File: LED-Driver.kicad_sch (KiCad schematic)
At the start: 9 parts, among them J1 Conn_01x04, J2 Barrel_Jack, Q1 Q_NPN_ECB, Q2 Q_NPN_ECB, Q3 Q_NPN_ECB, U1 Pico

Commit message: Add an initial PCB and swap out the barrel jack
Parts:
- removed J2: Barrel_Jack, Connector_BarrelJack:BarrelJack_SwitchcraftConxall_RAPC10U_Horizontal, symbol Connector:Barrel_Jack
- added J2: Barrel_Jack_Switch, Connector_BarrelJack:BarrelJack_CUI_PJ-102AH_Horizontal, symbol Connector:Barrel_Jack_Switch
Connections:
- net +12V: now also J2.1
- net GND: now also J2.2
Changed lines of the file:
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@@
+	)
+	(symbol
+		(lib_id "Connector:Barrel_Jack_Switch")
+		(at 25.4 88.9 0)
+		(unit 1)
+		(exclude_from_sim no)
+		(in_bom yes)
+		(on_board yes)
+		(dnp no)
+		(fields_autoplaced yes)
+		(property "Reference" "J2"
+			(at 25.4 80.01 0)
+			(effects
+				(font
+					(size 1.27 1.27)
+				)
+			)
+		)
+		(property "Value" "Barrel_Jack_Switch"
+			(at 25.4 82.55 0)
+			(effects
+				(font
+					(size 1.27 1.27)
+				)
+			)
+		)
+		(property "Footprint" "Connector_BarrelJack:BarrelJack_CUI_PJ-102AH_Horizontal"
+			(at 26.67 89.916 0)
+			(effects
+				(font
+					(size 1.27 1.27)
+				)
+				(hide yes)
+			)
+		)
+		(property "Datasheet" "~"
+			(at 26.67 89.916 0)
+			(effects
+				(font
+					(size 1.27 1.27)
+				)
+				(hide yes)
+			)
+		)
+		(property "Description" "DC Barrel Jack with an internal switch"
+			(at 25.4 88.9 0)
+			(effects
+				(font
+					(size 1.27 1.27)
+				)
+				(hide yes)
+			)
+		)
+		(pin "3"
+		)
+		(pin "2"
+		)
+		(pin "1"
+		)
+		(instances
+			(project ""
+				(path "/1411000f-ec3e-4037-9ea8-3f20f090e81e"
+					(reference "J2")
+					(unit 1)
+				)
+			)
+		)
 	)
 	(symbol
@@
 					(unit 1)
 				)
-			)
-		)
-	)
-	(symbol
-		(lib_id "Connector:Barrel_Jack")
-		(at 25.4 88.9 0)
-		(unit 1)
-		(exclude_from_sim no)
-		(in_bom yes)
-		(on_board yes)
-		(dnp no)
-		(fields_autoplaced yes)
-		(property "Reference" "J2"
-			(at 25.4 80.01 0)
-			(effects
-				(font
-					(size 1.27 1.27)
-				)
-			)
-		)
-		(property "Value" "Barrel_Jack"
-			(at 25.4 82.55 0)
-			(effects
-				(font
-					(size 1.27 1.27)
-				)
-			)
-		)
-		(property "Footprint" "Connector_BarrelJack:BarrelJack_SwitchcraftConxall_RAPC10U_Horizontal"
-			(at 26.67 89.916 0)
-			(effects
-				(font
-					(size 1.27 1.27)
-				)
-				(hide yes)
-			)
-		)
-		(property "Datasheet" "~"
-			(at 26.67 89.916 0)
-			(effects
-				(font
-					(size 1.27 1.27)
-				)
-				(hide yes)
-			)
-		)
-		(property "Description" "DC Barrel Jack"
-			(at 25.4 88.9 0)
-			(effects
-				(font
-					(size 1.27 1.27)
-				)
-				(hide yes)
-			)
-		)
-		(pin "1"
-		)
-		(pin "2"
-		)
-		(instances
-			(project ""
-				(path "/1411000f-ec3e-4037-9ea8-3f20f090e81e"
-					(reference "J2")
-					(unit 1)
-				)

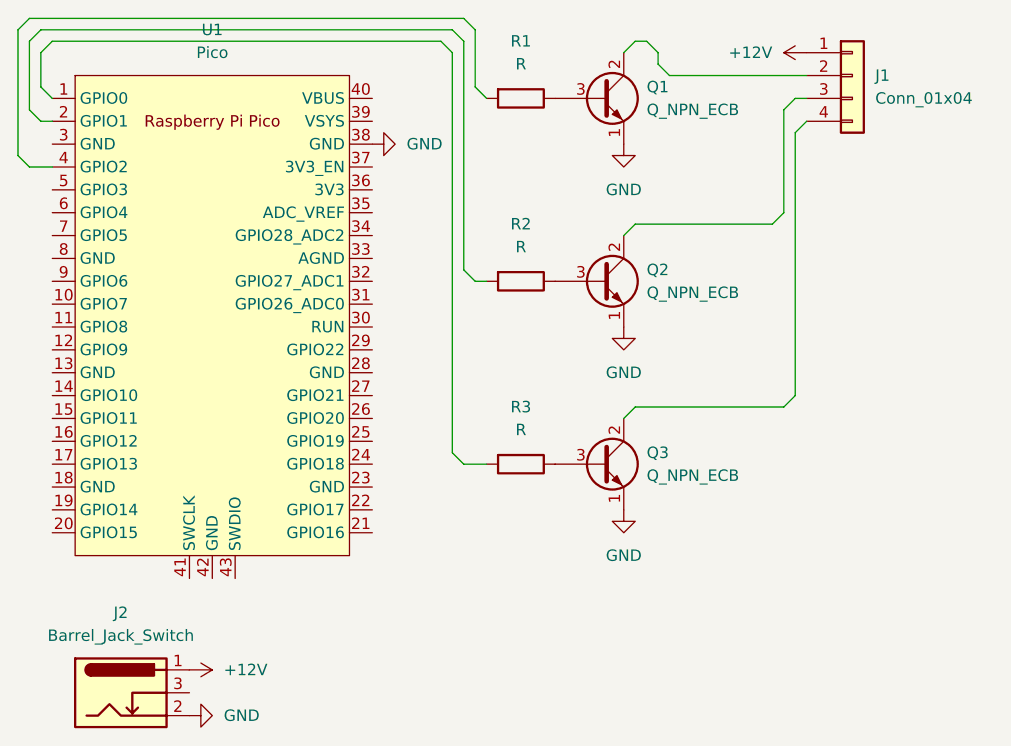
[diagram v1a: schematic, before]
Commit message: Add borders to the PCB
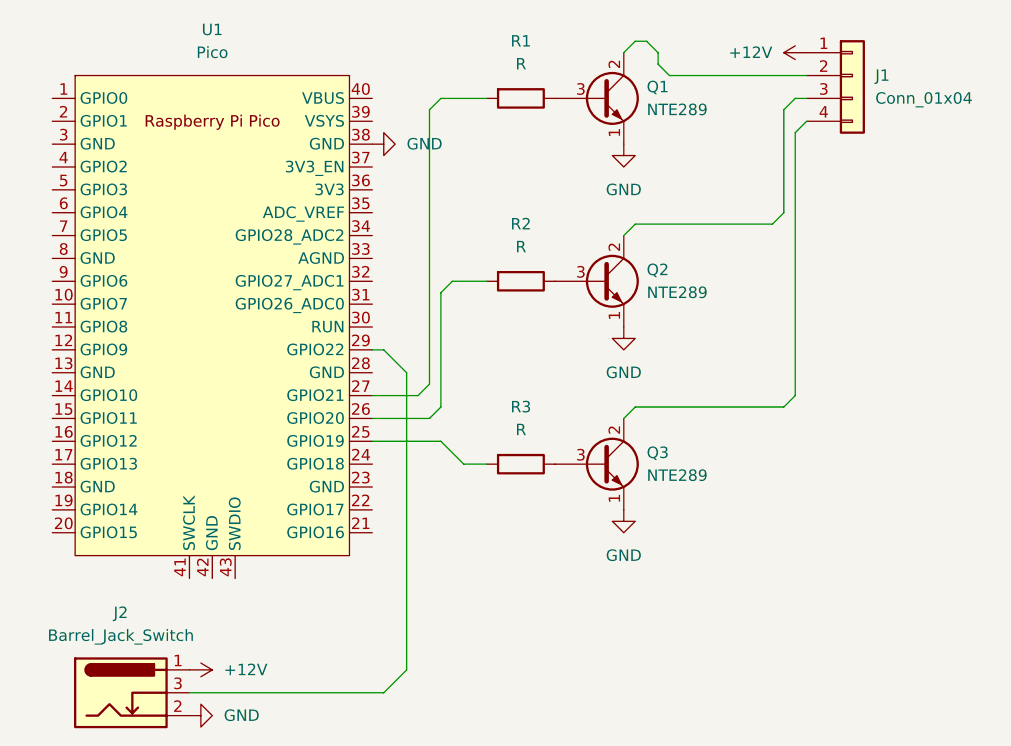
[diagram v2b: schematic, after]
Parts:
- J1: footprint (none) -> Connector_PinHeader_2.54mm:PinHeader_1x04_P2.54mm_Horizontal
- Q1, Q2, Q3: value Q_NPN_ECB -> NTE289; footprint (none) -> Package_TO_SOT_THT:TO-92_Inline
- R1, R2, R3: footprint (none) -> Resistor_THT:R_Axial_DIN0207_L6.3mm_D2.5mm_P10.16mm_Horizontal
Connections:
- net at R2.2: now also U1.26 (GPIO20); no longer U1.2 (GPIO1)
- net at U1.1 (GPIO0): no longer R3.2
- net at U1.25 (GPIO19): now also R3.2
- net at U1.27 (GPIO21): now also R1.2
- net at U1.29 (GPIO22): now also J2.3
- net at U1.4 (GPIO2): no longer R1.2
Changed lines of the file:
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@@
+	(wire
+		(pts
+			(xy 60.96 57.15) (xy 60.96 44.45)
+		)
+		(stroke
+			(width 0)
+			(type default)
+		)
+	)
 	(wire
 		(pts
@@
 	(wire
 		(pts
-			(xy 17.78 22.86) (xy 16.51 21.59)
-		)
-		(stroke
-			(width 0)
-			(type default)
-		)
-	)
-	(wire
-		(pts
-			(xy 64.77 43.18) (xy 63.5 41.91)
-		)
-		(stroke
-			(width 0)
-			(type default)
-		)
-	)
-	(wire
-		(pts
-			(xy 16.51 15.24) (xy 62.23 15.24)
+			(xy 58.42 55.88) (xy 59.69 54.61)
 		)
 		(stroke
@@
 	(wire
 		(pts
-			(xy 13.97 29.21) (xy 13.97 15.24)
-		)
-		(stroke
-			(width 0)
-			(type default)
-		)
-	)
-	(wire
-		(pts
 			(xy 82.55 16.51) (xy 83.82 16.51)
 		)
@@
 	(wire
 		(pts
-			(xy 64.77 15.24) (xy 63.5 13.97)
+			(xy 60.96 60.96) (xy 63.5 63.5)
 		)
 		(stroke
@@
 	(wire
 		(pts
-			(xy 13.97 15.24) (xy 15.24 13.97)
-		)
-		(stroke
-			(width 0)
-			(type default)
-		)
-	)
-	(wire
-		(pts
 			(xy 82.55 57.15) (xy 81.28 58.42)
 		)
@@
 	(wire
 		(pts
-			(xy 17.78 30.48) (xy 15.24 30.48)
+			(xy 53.34 50.8) (xy 54.61 50.8)
+		)
+		(stroke
+			(width 0)
+			(type default)
+		)
+	)
+	(wire
+		(pts
+			(xy 53.34 55.88) (xy 58.42 55.88)
 		)
 		(stroke
@@
 	(wire
 		(pts
-			(xy 15.24 13.97) (xy 63.5 13.97)
-		)
-		(stroke
-			(width 0)
-			(type default)
-		)
-	)
-	(wire
-		(pts
-			(xy 62.23 17.78) (xy 60.96 16.51)
-		)
-		(stroke
-			(width 0)
-			(type default)
-		)
-	)
-	(wire
-		(pts
-			(xy 15.24 16.51) (xy 16.51 15.24)
-		)
-		(stroke
-			(width 0)
-			(type default)
-		)
-	)
-	(wire
-		(pts
-			(xy 16.51 25.4) (xy 15.24 24.13)
-		)
-		(stroke
-			(width 0)
-			(type default)
-		)
-	)
-	(wire
-		(pts
-			(xy 66.04 43.18) (xy 64.77 43.18)
-		)
-		(stroke
-			(width 0)
-			(type default)
-		)
-	)
-	(wire
-		(pts
-			(xy 66.04 22.86) (xy 64.77 21.59)
-		)
-		(stroke
-			(width 0)
-			(type default)
-		)
-	)
-	(wire
-		(pts
-			(xy 16.51 17.78) (xy 17.78 16.51)
-		)
-		(stroke
-			(width 0)
-			(type default)
-		)
-	)
-	(wire
-		(pts
-			(xy 15.24 30.48) (xy 13.97 29.21)
-		)
-		(stroke
-			(width 0)
-			(type default)
-		)
-	)
-	(wire
-		(pts
-			(xy 17.78 25.4) (xy 16.51 25.4)
-		)
-		(stroke
-			(width 0)
-			(type default)
-		)
-	)
-	(wire
-		(pts
-			(xy 63.5 41.91) (xy 63.5 16.51)
-		)
-		(stroke
-			(width 0)
-			(type default)
-		)
-	)
-	(wire
-		(pts
-			(xy 63.5 16.51) (xy 62.23 15.24)
+			(xy 59.69 24.13) (xy 60.96 22.86)
 		)
 		(stroke
@@
 	(wire
 		(pts
+			(xy 60.96 22.86) (xy 66.04 22.86)
+		)
+		(stroke
+			(width 0)
+			(type default)
+		)
+	)
+	(wire
+		(pts
 			(xy 83.82 16.51) (xy 85.09 17.78)
 		)
@@
 	(wire
 		(pts
-			(xy 63.5 63.5) (xy 62.23 62.23)
-		)
-		(stroke
-			(width 0)
-			(type default)
-		)
-	)
-	(wire
-		(pts
 			(xy 81.28 17.78) (xy 82.55 16.51)
 		)
@@
 	(wire
 		(pts
-			(xy 64.77 21.59) (xy 64.77 15.24)
+			(xy 62.23 43.18) (xy 66.04 43.18)
 		)
 		(stroke
@@
 	(wire
 		(pts
-			(xy 16.51 17.78) (xy 16.51 21.59)
+			(xy 53.34 60.96) (xy 60.96 60.96)
 		)
 		(stroke
@@
 	(wire
 		(pts
+			(xy 57.15 53.34) (xy 57.15 86.36)
+		)
+		(stroke
+			(width 0)
+			(type default)
+		)
+	)
+	(wire
+		(pts
+			(xy 54.61 50.8) (xy 57.15 53.34)
+		)
+		(stroke
+			(width 0)
+			(type default)
+		)
+	)
+	(wire
+		(pts
 			(xy 99.06 57.15) (xy 82.55 57.15)
 		)
@@
 	(wire
 		(pts
+			(xy 59.69 54.61) (xy 59.69 24.13)
+		)
+		(stroke
+			(width 0)
+			(type default)
+		)
+	)
+	(wire
+		(pts
 			(xy 85.09 17.78) (xy 85.09 19.05)
 		)
@@
 	(wire
 		(pts
+			(xy 53.34 58.42) (xy 59.69 58.42)
+		)
+		(stroke
+			(width 0)
+			(type default)
+		)
+	)
+	(wire
+		(pts
 			(xy 100.33 26.67) (xy 100.33 55.88)
 		)
@@
 	(wire
 		(pts
-			(xy 15.24 24.13) (xy 15.24 16.51)
-		)
-		(stroke
-			(width 0)
-			(type default)
-		)
-	)
-	(wire
-		(pts
-			(xy 62.23 62.23) (xy 62.23 17.78)
-		)
-		(stroke
-			(width 0)
-			(type default)
-		)
-	)
-	(wire
-		(pts
-			(xy 17.78 16.51) (xy 60.96 16.51)
+			(xy 60.96 44.45) (xy 62.23 43.18)
+		)
+		(stroke
+			(width 0)
+			(type default)
+		)
+	)
+	(wire
+		(pts
+			(xy 57.15 86.36) (xy 54.61 88.9)
+		)
+		(stroke
+			(width 0)
+			(type default)
+		)
+	)
+	(wire
+		(pts
+			(xy 33.02 88.9) (xy 54.61 88.9)
+		)
+		(stroke
+			(width 0)
+			(type default)
+		)
+	)
+	(wire
+		(pts
+			(xy 59.69 58.42) (xy 60.96 57.15)
 		)
 		(stroke
@@
 			)
 		)
-		(property "Footprint" ""
+		(property "Footprint" "Resistor_THT:R_Axial_DIN0207_L6.3mm_D2.5mm_P10.16mm_Horizontal"
 			(at 69.85 41.402 90)
 			(effects
@@
 			)
 		)
-		(property "Footprint" ""
+		(property "Footprint" "Resistor_THT:R_Axial_DIN0207_L6.3mm_D2.5mm_P10.16mm_Horizontal"
 			(at 69.85 61.722 90)
 			(effects
@@
 			)
 		)
-		(property "Value" "Q_NPN_ECB"
+		(property "Value" "NTE289"
 			(at 83.82 24.1299 0)
 			(effects
@@
 			)
 		)
-		(property "Footprint" ""
+		(property "Footprint" "Package_TO_SOT_THT:TO-92_Inline"
 			(at 83.82 20.32 0)
 			(effects
@@
 			)
 		)
-		(property "Value" "Q_NPN_ECB"
+		(property "Value" "NTE289"
 			(at 83.82 44.4499 0)
 			(effects
@@
 			)
 		)
-		(property "Footprint" ""
+		(property "Footprint" "Package_TO_SOT_THT:TO-92_Inline"
 			(at 83.82 40.64 0)
 			(effects
@@
 			)
 		)
-		(property "Value" "Q_NPN_ECB"
+		(property "Value" "NTE289"
 			(at 83.82 64.7699 0)
 			(effects
@@
 			)
 		)
-		(property "Footprint" ""
+		(property "Footprint" "Package_TO_SOT_THT:TO-92_Inline"
 			(at 83.82 60.96 0)
 			(effects
@@
 			)
 		)
-		(property "Footprint" ""
+		(property "Footprint" "Connector_PinHeader_2.54mm:PinHeader_1x04_P2.54mm_Horizontal"
 			(at 106.68 20.32 0)
 			(effects
@@
 			)
 		)
-		(property "Footprint" ""
+		(property "Footprint" "Resistor_THT:R_Axial_DIN0207_L6.3mm_D2.5mm_P10.16mm_Horizontal"
 			(at 69.85 21.082 90)
 			(effects
